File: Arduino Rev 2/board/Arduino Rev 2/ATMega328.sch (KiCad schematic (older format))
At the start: 1 part, among them U201 ATMEGA328-AU

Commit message: finished Schematic
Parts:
- added D201, D202: LED, Arduino Rev 2:led, symbol arduino_symbols:LED
- added R201, R202: R_US, Arduino Rev 2:R_0603_1608Metric_Pad1.05x0.95mm_HandSolder, symbol arduino_symbols:R_US
- U201: footprint digikey-footprints:TQFP-32_7x7mm -> Arduino Rev 2:TQFP-32_7x7mm
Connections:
- net +5V: now also R201.1
- net D13_SCK: now also R202.1
- net GND: now also D201.1 (K), D202.1 (K)
- new net: D201.2 (A), R201.2
- new net: D202.2 (A), R202.2
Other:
- moved on the sheet: U201

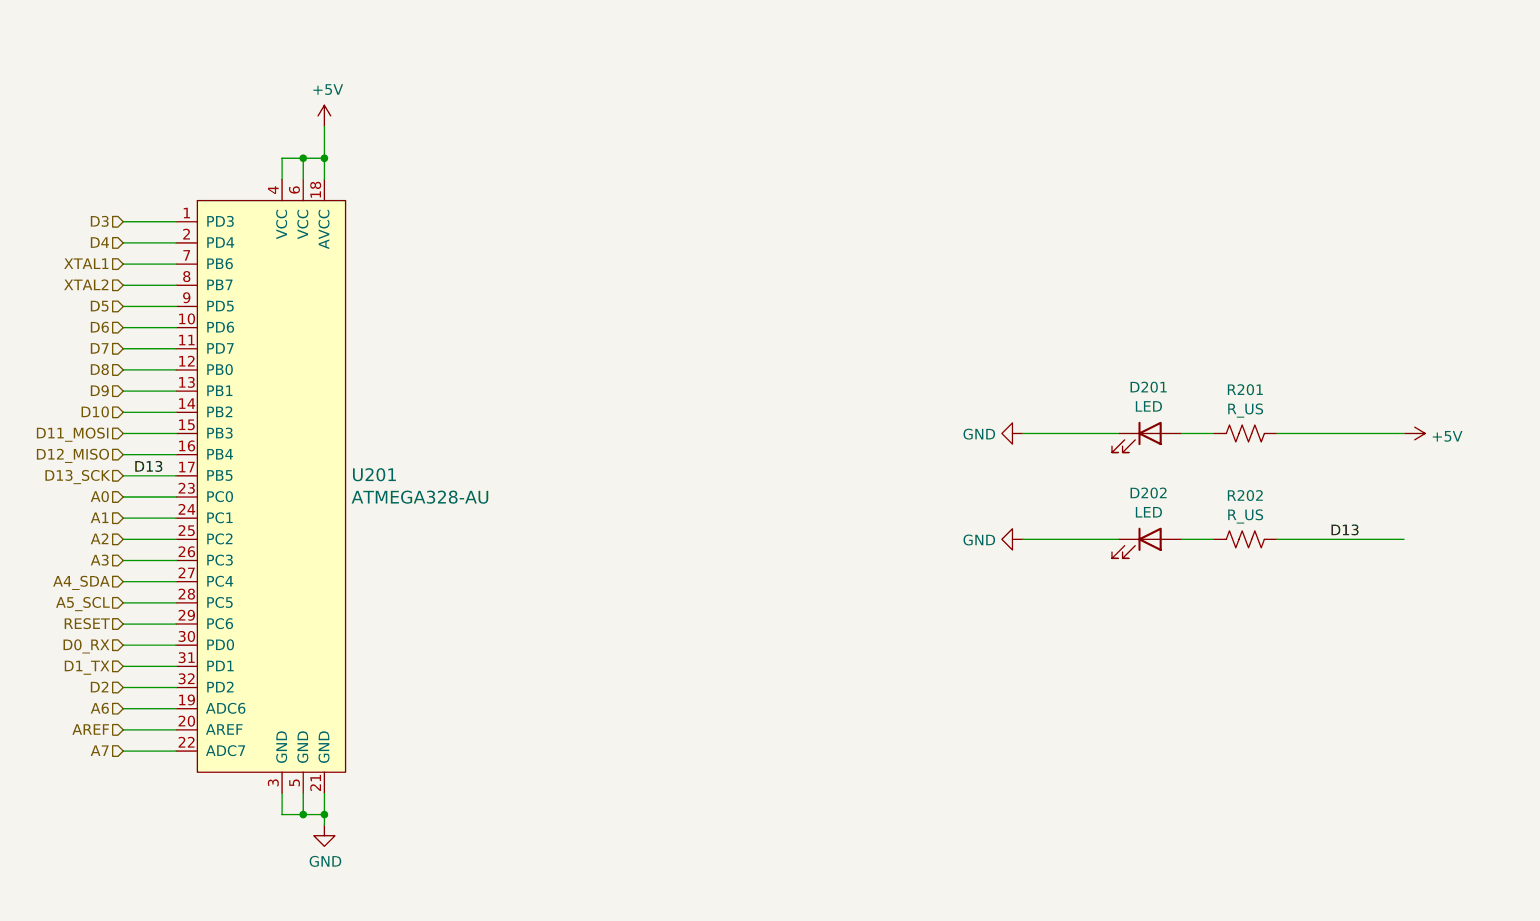
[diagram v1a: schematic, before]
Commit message: Fixed Schematic. Routing Finished
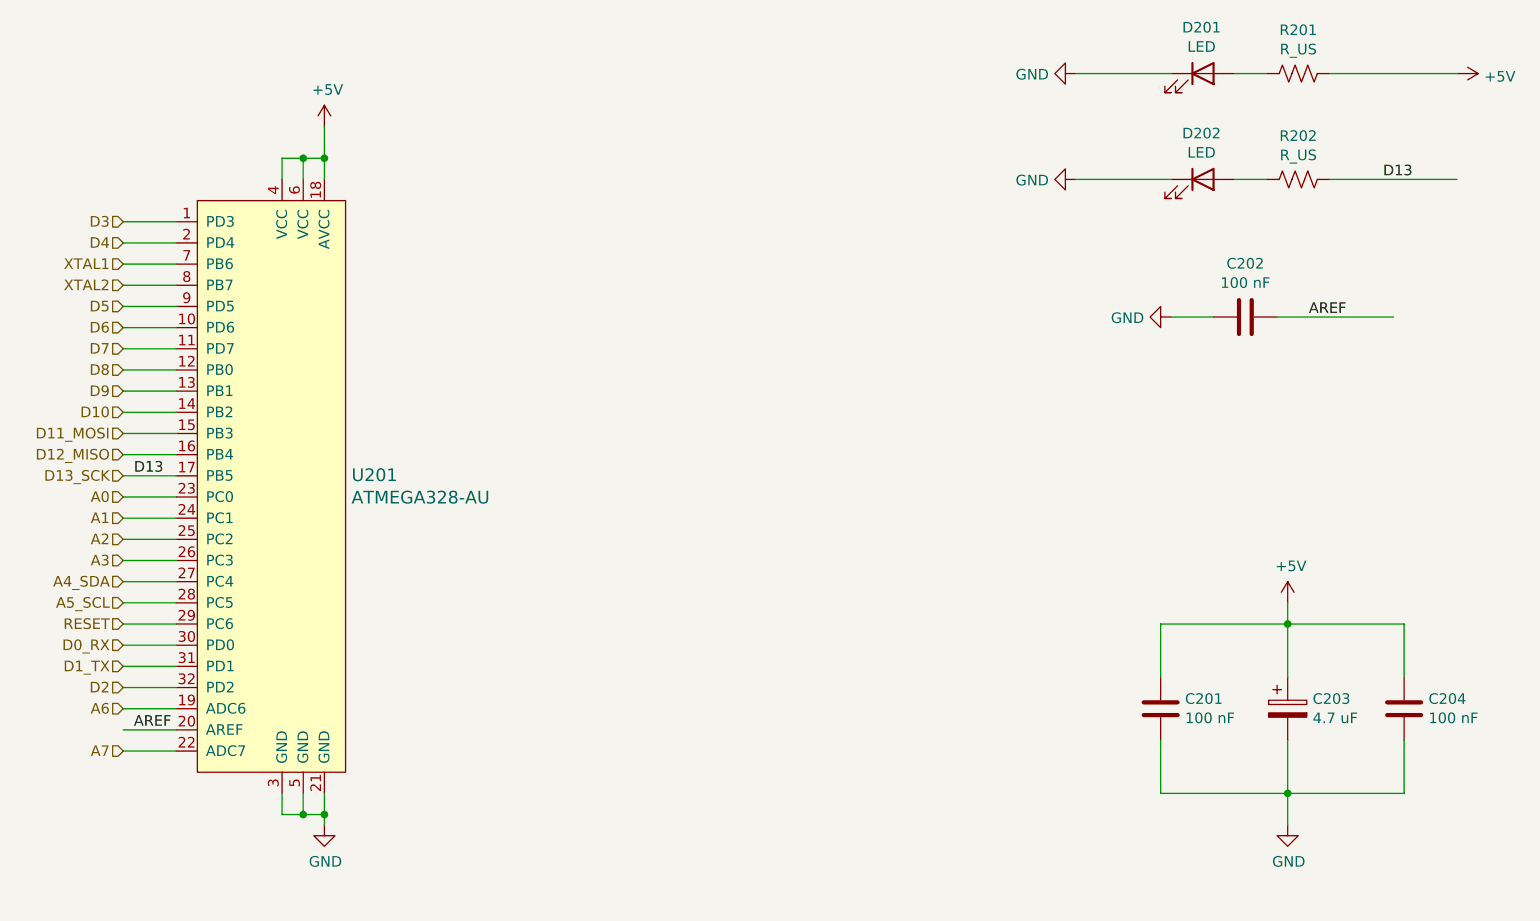
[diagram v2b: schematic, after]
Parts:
- added C201, C202, C204: 100 nF, Arduino Rev 2:C_0603_1608Metric_Pad1.05x0.95mm_HandSolder, symbol arduino_symbols:C
- added C203: 4.7 uF, Arduino Rev 2:CP_EIA-1608-10_AVX-L_Pad1.25x1.05mm_HandSolder, symbol Device:CP
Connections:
- wire segments 44 -> 58
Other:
- moved on the sheet: D201, D202, R201, R202
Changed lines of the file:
@@
 $Descr A4 11693 8268
 encoding utf-8
-Sheet 2 6
+Sheet 6 6
 Title ""
 Date ""
@@
 Text HLabel 2650 4500 0    50   Input ~ 0
 A6
-Text HLabel 2650 4600 0    50   Input ~ 0
-AREF
 Text HLabel 2650 4700 0    50   Input ~ 0
 A7
@@
 L arduino_symbols:LED D201
 U 1 1 5F0D775C
-P 7500 3200
-F 0 "D201" H 7493 3417 50  0000 C CNN
-F 1 "LED" H 7493 3326 50  0000 C CNN
-F 2 "Arduino Rev 2:led" H 7500 3200 50  0001 C CNN
-F 3 "~" H 7500 3200 50  0001 C CNN
-	1    7500 3200
+P 7750 1500
+F 0 "D201" H 7743 1717 50  0000 C CNN
+F 1 "LED" H 7743 1626 50  0000 C CNN
+F 2 "Arduino Rev 2:led" H 7750 1500 50  0001 C CNN
+F 3 "~" H 7750 1500 50  0001 C CNN
+	1    7750 1500
 	1    0    0    -1
 $EndComp
@@
 L arduino_symbols:LED D202
 U 1 1 5F0D806B
-P 7500 3700
-F 0 "D202" H 7493 3917 50  0000 C CNN
-F 1 "LED" H 7493 3826 50  0000 C CNN
-F 2 "Arduino Rev 2:led" H 7500 3700 50  0001 C CNN
-F 3 "~" H 7500 3700 50  0001 C CNN
-	1    7500 3700
+P 7750 2000
+F 0 "D202" H 7743 2217 50  0000 C CNN
+F 1 "LED" H 7743 2126 50  0000 C CNN
+F 2 "Arduino Rev 2:led" H 7750 2000 50  0001 C CNN
+F 3 "~" H 7750 2000 50  0001 C CNN
+	1    7750 2000
 	1    0    0    -1
 $EndComp
@@
 L arduino_symbols:R_US R201
 U 1 1 5F0D82EB
-P 7950 3200
-F 0 "R201" V 7745 3200 50  0000 C CNN
-F 1 "R_US" V 7836 3200 50  0000 C CNN
-F 2 "Arduino Rev 2:R_0603_1608Metric_Pad1.05x0.95mm_HandSolder" V 7990 3190 50  0001 C CNN
-F 3 "~" H 7950 3200 50  0001 C CNN
-	1    7950 3200
+P 8200 1500
+F 0 "R201" V 7995 1500 50  0000 C CNN
+F 1 "R_US" V 8086 1500 50  0000 C CNN
+F 2 "Arduino Rev 2:R_0603_1608Metric_Pad1.05x0.95mm_HandSolder" V 8240 1490 50  0001 C CNN
+F 3 "~" H 8200 1500 50  0001 C CNN
+	1    8200 1500
 	0    1    1    0
 $EndComp
@@
 L arduino_symbols:R_US R202
 U 1 1 5F0D89D0
-P 7950 3700
-F 0 "R202" V 7745 3700 50  0000 C CNN
-F 1 "R_US" V 7836 3700 50  0000 C CNN
-F 2 "Arduino Rev 2:R_0603_1608Metric_Pad1.05x0.95mm_HandSolder" V 7990 3690 50  0001 C CNN
-F 3 "~" H 7950 3700 50  0001 C CNN
-	1    7950 3700
+P 8200 2000
+F 0 "R202" V 7995 2000 50  0000 C CNN
+F 1 "R_US" V 8086 2000 50  0000 C CNN
+F 2 "Arduino Rev 2:R_0603_1608Metric_Pad1.05x0.95mm_HandSolder" V 8240 1990 50  0001 C CNN
+F 3 "~" H 8200 2000 50  0001 C CNN
+	1    8200 2000
 	0    1    1    0
 $EndComp
@@
 D13
 Wire Wire Line
-	7650 3200 7800 3200
-Wire Wire Line
-	7650 3700 7800 3700
+	7900 1500 8050 1500
+Wire Wire Line
+	7900 2000 8050 2000
 $Comp
 L power:GND #PWR0203
 U 1 1 5F0DE75F
-P 6900 3200
-F 0 "#PWR0203" H 6900 2950 50  0001 C CNN
-F 1 "GND" V 6905 3072 50  0000 R CNN
-F 2 "" H 6900 3200 50  0001 C CNN
-F 3 "" H 6900 3200 50  0001 C CNN
-	1    6900 3200
+P 7150 1500
+F 0 "#PWR0203" H 7150 1250 50  0001 C CNN
+F 1 "GND" V 7155 1372 50  0000 R CNN
+F 2 "" H 7150 1500 50  0001 C CNN
+F 3 "" H 7150 1500 50  0001 C CNN
+	1    7150 1500
 	0    1    1    0
 $EndComp
@@
 L power:GND #PWR0204
 U 1 1 5F0DEAA3
-P 6900 3700
-F 0 "#PWR0204" H 6900 3450 50  0001 C CNN
-F 1 "GND" V 6905 3572 50  0000 R CNN
-F 2 "" H 6900 3700 50  0001 C CNN
-F 3 "" H 6900 3700 50  0001 C CNN
-	1    6900 3700
-	0    1    1    0
-$EndComp
-Wire Wire Line
-	6900 3200 7350 3200
-Wire Wire Line
-	7350 3700 6900 3700
-Wire Wire Line
-	8100 3700 8700 3700
-Wire Wire Line
-	8100 3200 8700 3200
-$Comp
-L power:+5V #PWR0205
+P 7150 2000
+F 0 "#PWR0204" H 7150 1750 50  0001 C CNN
+F 1 "GND" V 7155 1872 50  0000 R CNN
+F 2 "" H 7150 2000 50  0001 C CNN
+F 3 "" H 7150 2000 50  0001 C CNN
+	1    7150 2000
+	0    1    1    0
+$EndComp
+Wire Wire Line
+	7150 1500 7600 1500
+Wire Wire Line
+	7600 2000 7150 2000
+Wire Wire Line
+	8350 2000 8950 2000
+Wire Wire Line
+	8350 1500 8950 1500
+$Comp
+L power:+5V #PWR0208
 U 1 1 5F0E14C4
-P 8700 3200
-F 0 "#PWR0205" H 8700 3050 50  0001 C CNN
-F 1 "+5V" V 8715 3328 50  0000 L CNN
-F 2 "" H 8700 3200 50  0001 C CNN
-F 3 "" H 8700 3200 50  0001 C CNN
-	1    8700 3200
-	0    1    1    0
-$EndComp
-Text Label 8350 3700 0    50   ~ 0
+P 8950 1500
+F 0 "#PWR0208" H 8950 1350 50  0001 C CNN
+F 1 "+5V" V 8965 1628 50  0000 L CNN
+F 2 "" H 8950 1500 50  0001 C CNN
+F 3 "" H 8950 1500 50  0001 C CNN
+	1    8950 1500
+	0    1    1    0
+$EndComp
+Text Label 8600 2000 0    50   ~ 0
 D13
+$Comp
+L arduino_symbols:C C202
+U 1 1 5F0E213A
+P 7950 2650
+F 0 "C202" V 7698 2650 50  0000 C CNN
+F 1 "100 nF" V 7789 2650 50  0000 C CNN
+F 2 "Arduino Rev 2:C_0603_1608Metric_Pad1.05x0.95mm_HandSolder" H 7988 2500 50  0001 C CNN
+F 3 "~" H 7950 2650 50  0001 C CNN
+	1    7950 2650
+	0    1    1    0
+$EndComp
+Text Label 2700 4600 0    50   ~ 0
+AREF
+$Comp
+L power:GND #PWR0205
+U 1 1 5F0E3930
+P 7600 2650
+F 0 "#PWR0205" H 7600 2400 50  0001 C CNN
+F 1 "GND" V 7605 2522 50  0000 R CNN
+F 2 "" H 7600 2650 50  0001 C CNN
+F 3 "" H 7600 2650 50  0001 C CNN
+	1    7600 2650
+	0    1    1    0
+$EndComp
+Wire Wire Line
+	7600 2650 7800 2650
+Wire Wire Line
+	8100 2650 8650 2650
+Text Label 8250 2650 0    50   ~ 0
+AREF
+$Comp
+L arduino_symbols:C C201
+U 1 1 5F0E66ED
+P 7550 4500
+F 0 "C201" H 7435 4454 50  0000 R CNN
+F 1 "100 nF" H 7435 4545 50  0000 R CNN
+F 2 "Arduino Rev 2:C_0603_1608Metric_Pad1.05x0.95mm_HandSolder" H 7588 4350 50  0001 C CNN
+F 3 "~" H 7550 4500 50  0001 C CNN
+	1    7550 4500
+	-1   0    0    1
+$EndComp
+$Comp
+L arduino_symbols:C C204
+U 1 1 5F0E6FF2
+P 8700 4500
+F 0 "C204" H 8585 4454 50  0000 R CNN
+F 1 "100 nF" H 8585 4545 50  0000 R CNN
+F 2 "Arduino Rev 2:C_0603_1608Metric_Pad1.05x0.95mm_HandSolder" H 8738 4350 50  0001 C CNN
+F 3 "~" H 8700 4500 50  0001 C CNN
+	1    8700 4500
+	-1   0    0    1
+$EndComp
+$Comp
+L Device:CP C203
+U 1 1 5F0E7368
+P 8150 4500
+F 0 "C203" H 8268 4546 50  0000 L CNN
+F 1 "4.7 uF" H 8268 4455 50  0000 L CNN
+F 2 "Arduino Rev 2:CP_EIA-1608-10_AVX-L_Pad1.25x1.05mm_HandSolder" H 8188 4350 50  0001 C CNN
+F 3 "~" H 8150 4500 50  0001 C CNN
+F 4 "478-8651-1-ND" H 8150 4500 50  0001 C CNN "Digikey"
+	1    8150 4500
+	1    0    0    -1
+$EndComp
+$Comp
+L power:+5V #PWR0206
+U 1 1 5F0E7E78
+P 8150 4000
+F 0 "#PWR0206" H 8150 3850 50  0001 C CNN
+F 1 "+5V" H 8165 4173 50  0000 C CNN
+F 2 "" H 8150 4000 50  0001 C CNN
+F 3 "" H 8150 4000 50  0001 C CNN
+	1    8150 4000
+	1    0    0    -1
+$EndComp
+Wire Wire Line
+	7550 4350 7550 4100
+Wire Wire Line
+	7550 4100 8150 4100
+Wire Wire Line
+	8150 4350 8150 4100
+Connection ~ 8150 4100
+Wire Wire Line
+	8150 4100 8150 4000
+$Comp
+L power:GND #PWR0207
+U 1 1 5F0E9F50
+P 8150 5050
+F 0 "#PWR0207" H 8150 4800 50  0001 C CNN
+F 1 "GND" H 8155 4877 50  0000 C CNN
+F 2 "" H 8150 5050 50  0001 C CNN
+F 3 "" H 8150 5050 50  0001 C CNN
+	1    8150 5050
+	1    0    0    -1
+$EndComp
+Wire Wire Line
+	7550 4650 7550 4900
+Wire Wire Line
+	7550 4900 8150 4900
+Wire Wire Line
+	8150 4650 8150 4900
+Connection ~ 8150 4900
+Wire Wire Line
+	8150 5050 8150 4900
+Wire Wire Line
+	8700 4900 8700 4650
+Wire Wire Line
+	8150 4900 8700 4900
+Wire Wire Line
+	8700 4350 8700 4100
+Wire Wire Line
+	8150 4100 8700 4100
 $EndSCHEMATC

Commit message: Final Board Design
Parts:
- D201, D202: Digikey (none) -> LTST-C171KGKT
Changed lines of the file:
@@
 F 2 "Arduino Rev 2:led" H 7750 1500 50  0001 C CNN
 F 3 "~" H 7750 1500 50  0001 C CNN
+F 4 "LTST-C171KGKT" H 7750 1500 50  0001 C CNN "Digikey"
 	1    7750 1500
 	1    0    0    -1
@@
 F 2 "Arduino Rev 2:led" H 7750 2000 50  0001 C CNN
 F 3 "~" H 7750 2000 50  0001 C CNN
+F 4 "LTST-C171KGKT" H 7750 2000 50  0001 C CNN "Digikey"
 	1    7750 2000
 	1    0    0    -1
